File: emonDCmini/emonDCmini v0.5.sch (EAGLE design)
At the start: 26 parts, among them J1 1X2-3.5MM, J2 1X2-3.5MM, Q2 DS18B20

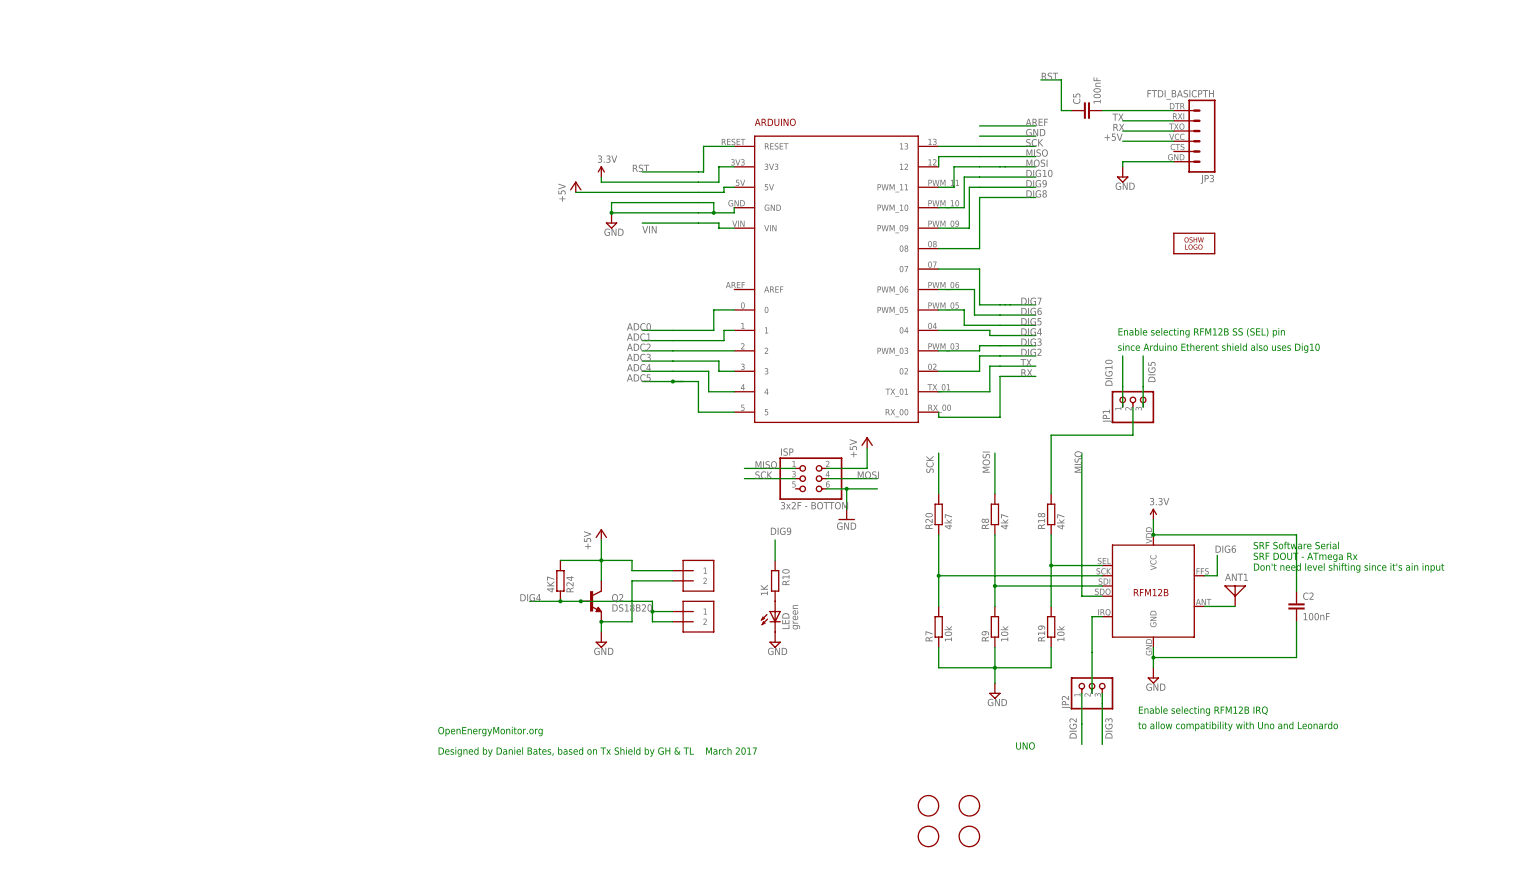
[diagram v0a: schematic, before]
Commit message: update
chip select set to GPIO4 for both mini and duo.
mini updated, various minor changes for v0.5.
molex micro sd card library improved
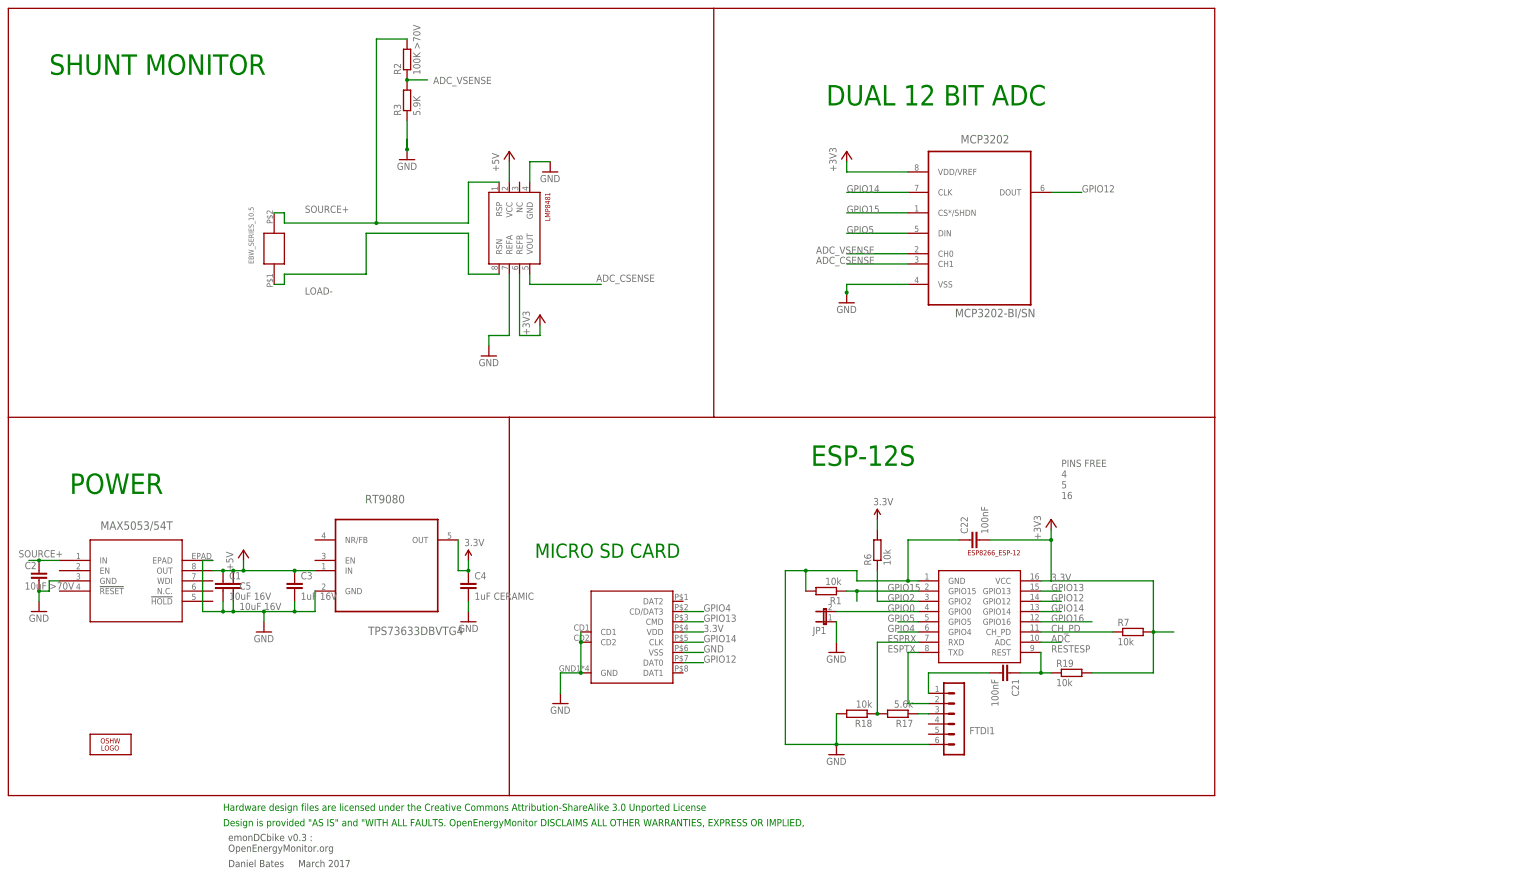
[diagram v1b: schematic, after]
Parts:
- removed ANT1: (no value), discrete:ANTENNA
- removed ARDUINO1: ARDUINO2, arduino:ARDUINO2
- removed ISP: 3x2F - BOTTOM, pinhead:PINHD-2X3
- removed J1, J2: 1X2-3.5MM, adafruit:1X2-3.5MM
- removed JP2: (no value), adafruit:PINHD-1X3
- removed JP3: FTDI_BASICPTH, SparkFun:FTDI_BASICPTH
- removed LED: green, led:LEDCHIPLED_0805
- removed Q2: DS18B20, SparkFun:TRANSISTOR_NPNTO92
- removed R10: 1K, rcl:R-EU_R0603
- removed R20, R8: 4k7, rcl:R-EU_R0603
- removed R24: 4K7, rcl:R-EU_R0603
- removed R9: 10k, rcl:R-EU_R0603
- removed U$1, U$3, U$4, U$5: FIDUCIAL, adafruit:FIDUCIAL
- added C1: 10uF 16V, rcl:C-EUC0603
- added C21, C22: 100nF, rcl:C-EUC0603
- added C3: 1uF 16V, rcl:C-EUC0603
- added C4: 1uF CERAMIC, rcl:C-EUC0603
- added EBW_SERIES_10.5: EBW_SERIES_10.5MM, EBW series shunt:EBW_SERIES_10.5MM
- added ESP-12: ESP8266_ESP-12, ESP8266-ESP12:ESP8266_ESP-12
- added FTDI1: FTDI-ESP, JeeLabs:MA06-1
- added LMP8481: LMP8481-H, lmp8481b:LMP8481LMP8481-H
- added MAX5053: MAX5023TASA-T21-0111D_SBE-14-L, MAX5053:MAX5023TASA-T21-0111D_SBE-14-L
- added MCP3202: MCP3202-BI/SN, Microchip-MCP3202-BI_SN:MCP3202-BI/SN
- added R1, R6: 10k, rcl:R-EU_R0603
- added R17: 5.6k, rcl:R-EU_R0603
- added R2: 100K >70V, rcl:R-EU_R0603
- added R3: 5.9K, rcl:R-EU_R0603
- added RT9080: TPS73633DBVTG4, TSOT-23-5 REGULATOR 3.3v:TPS73633DBVTG4
- C2: value 100nF -> 10uF >70V
- C5: value 100nF -> 10uF 16V
- JP1: device adafruit:PINHD-1X3 -> jumper:JP1E
- LOGO1: value OSHW_LOGO_10MILX0200-NT -> OSHW_LOGO_6MILX0200-NT; device ohw-logo:OSHW_LOGO_10MILX0200-NT -> ohw-logo:OSHW_LOGO_6MILX0200-NT; OC_FARNELL (none) -> unknown
- R18: value 4k7 -> 10k
- U$2: value RFM12B -> MOLEX_MICRO_SD_1040310811; device lh-library:RFM12B -> MOLEX MICRO SD [exposed pins]:MOLEX_MICRO_SD_1040310811
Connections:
- removed net ADC0: ARDUINO1.0
- removed net ADC1: ARDUINO1.1
- removed net ADC2: ARDUINO1.2
- removed net ADC3: ARDUINO1.3
- removed net ADC4: ARDUINO1.4
- removed net ADC5: ARDUINO1.5
- removed net DIG10: ARDUINO1.PWM_10, JP1.1
- removed net DIG2: ARDUINO1.02, JP2.1
- removed net DIG3: ARDUINO1.PWM_03, JP2.3
- removed net DIG4: ARDUINO1.04, J2.1, J2.2, Q2.B, R24.2
- removed net DIG5: ARDUINO1.PWM_05, JP1.3
- removed net DIG6: ARDUINO1.PWM_06, U$2.FFS
- removed net DIG7: ARDUINO1.07
- removed net DIG8: ARDUINO1.08
- removed net DIG9: ARDUINO1.PWM_09, R10.2
- removed net MISO: ARDUINO1.12, ISP.1, U$2.SDO
- removed net MOSI: ARDUINO1.PWM_11, ISP.4, R8.2
- removed net N$1: JP2.2, U$2.IRQ
- removed net N$12: C5.2, JP3.1
- removed net N$2: JP1.2, R18.2
- removed net N$41: LED.A, R10.1
- removed net N$42: ANT1.1, U$2.ANT
- removed net N$43: R20.1, R7.2, U$2.SCK
- removed net N$44: R8.1, R9.2, U$2.SDI
- removed net N$45: R18.1, R19.2, U$2.SEL
- removed net RX: ARDUINO1.RX_00, JP3.3
- removed net SCK: ARDUINO1.13, ISP.3, R20.2
- removed net TX: ARDUINO1.TX_01, JP3.2
- removed net VIN: ARDUINO1.VIN
- new net ADC: ESP-12.ADC
- new net ADC_CSENSE: LMP8481.VOUT, MCP3202.CH1
- new net ADC_VSENSE: MCP3202.CH0, R2.1, R3.2
- new net CH_PD: ESP-12.CH_PD, R7.1
- new net ESPRX: ESP-12.RXD, R17.2, R18.1
- new net ESPTX: ESP-12.TXD, FTDI1.2
- new net GPIO0: ESP-12.GPIO0, JP1.2
- new net GPIO12: ESP-12.GPIO12, MCP3202.DOUT, U$2.DAT0
- new net GPIO13: ESP-12.GPIO13, U$2.CMD
- new net GPIO14: ESP-12.GPIO14, MCP3202.CLK, U$2.CLK
- new net GPIO15: ESP-12.GPIO15, MCP3202.CS*/SHDN, R1.1
- new net GPIO16: ESP-12.GPIO16
- new net GPIO2: ESP-12.GPIO2, R6.1
- new net GPIO4: ESP-12.GPIO4, U$2.CD/DAT3
- new net GPIO5: ESP-12.GPIO5, MCP3202.DIN
- new net LOAD-: EBW_SERIES_10.5.P$1, LMP8481.RSN
- new net N$36: FTDI1.3, R17.1
- new net RESTESP: C21.1, ESP-12.REST, R19.1
- new net SOURCE+: C2.1, EBW_SERIES_10.5.P$2, LMP8481.RSP, MAX5053.IN, R2.2
- net +5V: now also C1.1, C3.1, C5.1, MAX5053.OUT, RT9080.IN; no longer ARDUINO1.5V, ISP.2, J1.1, JP3.4, Q2.C, R24.1
- net 3.3V: now also C22.2, C4.1, ESP-12.VCC, LMP8481.REFB, MCP3202.VDD/VREF, R19.2, R6.2, R7.2, RT9080.OUT, U$2.VDD; no longer ARDUINO1.3V3, C2.1, U$2.VCC
- net GND: now also C1.2, C22.1, C3.2, C4.2, C5.2, ESP-12.GND, FTDI1.6, JP1.1, LMP8481.GND, LMP8481.REFA, MAX5053.EPAD, MAX5053.GND, MCP3202.VSS, R1.2, R18.2, R3.1, RT9080.GND, U$2.CD1, U$2.CD2, U$2.VSS; no longer ARDUINO1.GND, ISP.6, J1.2, JP3.6, LED.C, Q2.E, R19.1, R7.1, R9.1
- net RST: now also C21.2, FTDI1.1; no longer ARDUINO1.RESET, C5.1
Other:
- note added: "DUAL 12 BIT ADC"
- note added: "Daniel Bates March 2017"
- note added: "Design is provided "AS IS" and "WITH ALL FAULTS. OpenEnergyMonitor DISCLAIMS ALL OTHER WARRANTIES, EXPRESS OR IMPLIED,"
- note added: "ESP-12S"
- note added: "Hardware design files are licensed under the Creative Commons Attribution-ShareAlike 3.0 Unported License"
- note added: "MICRO SD CARD"
- note added: "PINS FREE 4 5 16"
- note added: "POWER"
- note added: "SHUNT MONITOR"
- note added: "emonDCbike v0.3 : OpenEnergyMonitor.org"
- note removed: "Designed by Daniel Bates, based on Tx Shield by GH & TL March 2017"
- note removed: "Enable selecting RFM12B IRQ"
- note removed: "Enable selecting RFM12B SS (SEL) pin"
- note removed: "OpenEnergyMonitor.org"
- note removed: "SRF Software Serial SRF DOUT - ATmega Rx Don't need level shifting since it's ain input"
- note removed: "UNO"
- note removed: "since Arduino Etherent shield also uses Dig10"
- note removed: "to allow compatibility with Uno and Leonardo"
- moved on the sheet: C2, C5, R18, R19, R7
